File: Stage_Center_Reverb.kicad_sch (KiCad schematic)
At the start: 43 parts, among them J1 Input, J2 Output, J3 ToTank, J4 FromTank, J5 DC9V, Q1 2N3906, SW1 SW_SPDT, SW2 SW_SPDT, SW3 SW_SPDT, SW4 kill, U1 TL072, U2 TL072, U3 MAX1044

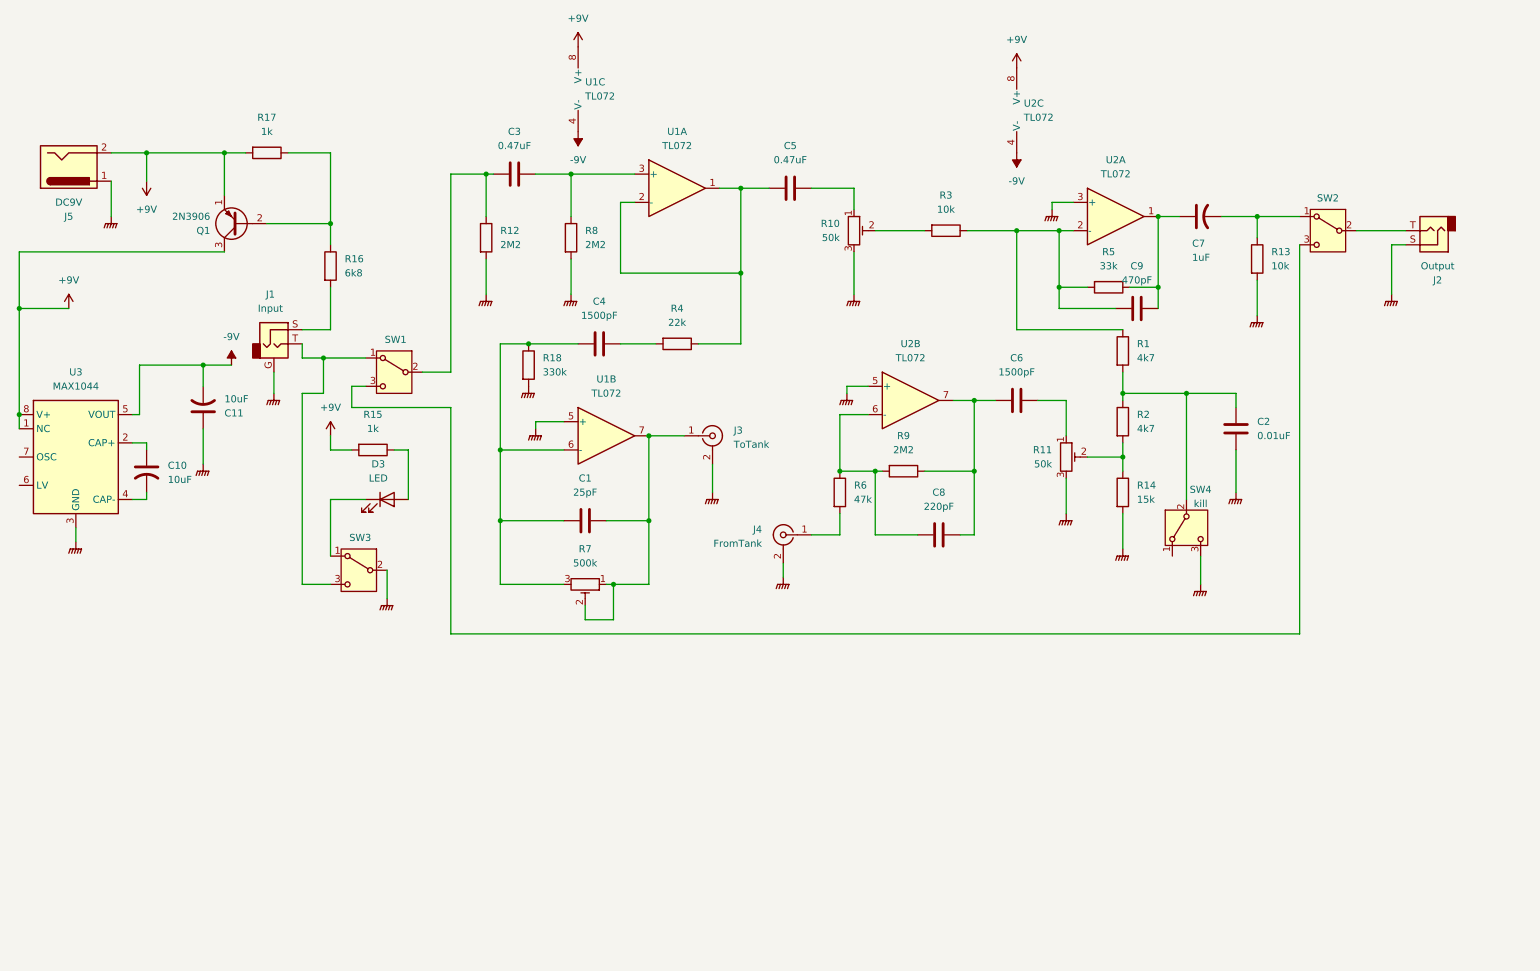
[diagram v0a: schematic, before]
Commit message: 電源部分を変更
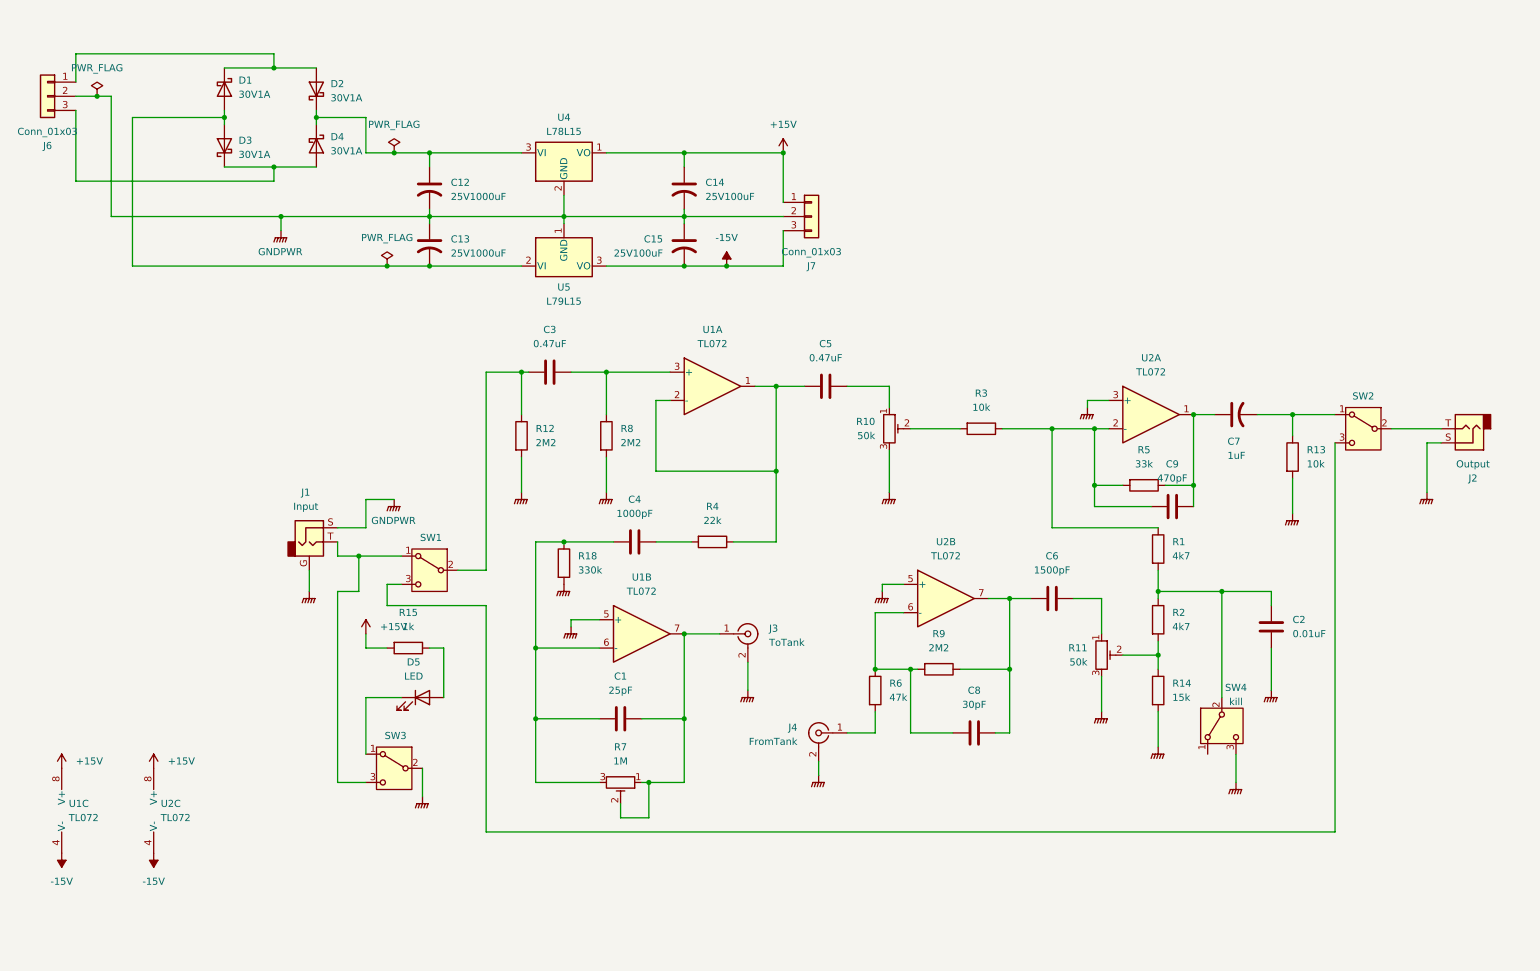
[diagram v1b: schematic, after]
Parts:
- removed C10, C11: 10uF, Capacitor_THT:CP_Radial_D6.3mm_P2.50mm, symbol Device:C_US
- removed J5: DC9V, symbol Connector:Jack-DC
- removed Q1: 2N3906, Package_TO_SOT_THT:TO-92_Inline, symbol Transistor_BJT:2N3906
- removed R16: 6k8, Resistor_THT:R_Axial_DIN0207_L6.3mm_D2.5mm_P7.62mm_Horizontal, symbol Device:R
- removed R17: 1k, Resistor_THT:R_Axial_DIN0207_L6.3mm_D2.5mm_P7.62mm_Horizontal, symbol Device:R
- removed U3: MAX1044, Package_DIP:DIP-8_W7.62mm_Socket, symbol Regulator_SwitchedCapacitor:MAX1044
- added C12, C13: 25V1000uF, Capacitor_THT:CP_Radial_D10.0mm_P5.00mm, symbol Device:C_US
- added C14, C15: 25V100uF, Capacitor_THT:CP_Radial_D7.5mm_P2.50mm, symbol Device:C_US
- added D1, D2, D3, D4: 30V1A, Diode_THT:D_DO-41_SOD81_P10.16mm_Horizontal, symbol Diode:1N5817
- added J6, J7: Conn_01x03, Connector_JST:JST_XH_B3B-XH-A_1x03_P2.50mm_Vertical, symbol Connector_Generic:Conn_01x03
- added U4: L78L15, Package_TO_SOT_THT:TO-92_Inline_Wide, symbol Regulator_Linear:L78L12_TO92
- added U5: L79L15, Package_TO_SOT_THT:TO-92_Inline_Wide, symbol Regulator_Linear:L79L12_TO92
- C4: value 1500pF -> 1000pF
- C8: value 220pF -> 30pF
- R7: value 500k -> 1M
- renumbered D3 to D5
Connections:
- net GNDPWR: now also J1.S, C12.2, C13.1, C14.2, C15.1, J6.2 (Pin_2), J7.2 (Pin_2), U4.2 (GND), U5.1 (GND)
- net +9V renamed +15V
- net +15V: now also C14.1, J7.1 (Pin_1), U4.1 (VO)
- net -9V renamed -15V
- net -15V: now also C15.2, J7.3 (Pin_3), U5.3 (VO)
- new net: C12.1, D2.1 (K), D4.1 (K), U4.3 (VI)
- new net: D1.1 (K), D2.2 (A), J6.1 (Pin_1)
- new net: C13.2, D1.2 (A), D3.2 (A), U5.2 (VI)
- new net: D3.1 (K), D4.2 (A), J6.3 (Pin_3)
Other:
- moved on the sheet: C1, C2, C3, C4, C5, C6, C7, C8, C9, D5, J1, J2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

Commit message: パーツを小型化したフットプリント
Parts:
- C2: footprint @MyLibrary:7.5_3.5_p5.0 -> Capacitor_THT:C_Rect_L7.2mm_W2.5mm_P5.00mm_FKS2_FKP2_MKS2_MKP2
- C3, C5, C6: footprint @MyLibrary:7.5_3.5_p5.0 -> Capacitor_THT:C_Rect_L7.2mm_W3.5mm_P5.00mm_FKS2_FKP2_MKS2_MKP2
- C4: footprint @MyLibrary:7.5_3.5_p5.0 -> Capacitor_THT:C_Disc_D6.0mm_W2.5mm_P5.00mm
- C7: footprint @MyLibrary:10.5_5.0_p7.5 -> Capacitor_THT:C_Rect_L10.3mm_W5.0mm_P7.50mm_MKS4
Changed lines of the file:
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@@
 			)
 		)
-		(property "Footprint" "@MyLibrary:7.5_3.5_p5.0"
+		(property "Footprint" "Capacitor_THT:C_Rect_L7.2mm_W3.5mm_P5.00mm_FKS2_FKP2_MKS2_MKP2"
 			(at 167.64 80.3148 0)
 			(effects
@@
 			)
 		)
-		(property "Footprint" "@MyLibrary:10.5_5.0_p7.5"
+		(property "Footprint" "Capacitor_THT:C_Rect_L10.3mm_W5.0mm_P7.50mm_MKS4"
 			(at 237.49 86.36 0)
 			(effects
@@
 			)
 		)
-		(property "Footprint" "@MyLibrary:7.5_3.5_p5.0"
+		(property "Footprint" "Capacitor_THT:C_Rect_L7.2mm_W3.5mm_P5.00mm_FKS2_FKP2_MKS2_MKP2"
 			(at 208.28 118.4148 0)
 			(effects
@@
 			)
 		)
-		(property "Footprint" "@MyLibrary:7.5_3.5_p5.0"
+		(property "Footprint" "Capacitor_THT:C_Rect_L7.2mm_W2.5mm_P5.00mm_FKS2_FKP2_MKS2_MKP2"
 			(at 244.8052 128.27 0)
 			(effects
@@
 			)
 		)
-		(property "Footprint" "@MyLibrary:7.5_3.5_p5.0"
+		(property "Footprint" "Capacitor_THT:C_Disc_D6.0mm_W2.5mm_P5.00mm"
 			(at 133.35 108.2548 0)
 			(effects
@@
 			)
 		)
-		(property "Footprint" "@MyLibrary:7.5_3.5_p5.0"
+		(property "Footprint" "Capacitor_THT:C_Rect_L7.2mm_W3.5mm_P5.00mm_FKS2_FKP2_MKS2_MKP2"
 			(at 118.11 77.7748 0)
 			(effects

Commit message: フットプリント修正、LEDの抵抗を可変に変更
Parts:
- removed R15: 1k, Resistor_THT:R_Axial_DIN0207_L6.3mm_D2.5mm_P7.62mm_Horizontal, symbol Device:R
- added RV1: 1k, Potentiometer_THT:Potentiometer_Vishay_T73YP_Vertical, symbol Device:R_Potentiometer_Trim
- renumbered R7 to RV2, R10 to RV3, R11 to RV4
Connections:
- net +15V: now also RV1.2
- net GNDPWR: now also RV1.1
- net at D5.2 (A): now also RV1.3
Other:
- moved on the sheet: D5, SW3
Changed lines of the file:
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@@
 	(wire
 		(pts
-			(xy 81.28 137.16) (xy 81.28 147.32)
+			(xy 81.28 144.78) (xy 81.28 154.94)
 		)
 		(stroke
@@
 	(wire
 		(pts
-			(xy 91.44 149.86) (xy 91.44 154.94)
+			(xy 91.44 157.48) (xy 91.44 162.56)
 		)
 		(stroke
@@
 	(wire
 		(pts
-			(xy 76.2 118.11) (xy 76.2 152.4)
-		)
-		(stroke
-			(width 0)
-			(type default)
-		)
-	)
-	(wire
-		(pts
-			(xy 87.63 137.16) (xy 81.28 137.16)
+			(xy 87.63 144.78) (xy 81.28 144.78)
 		)
 		(stroke
@@
 	(wire
 		(pts
+			(xy 88.9 124.46) (xy 95.25 124.46)
+		)
+		(stroke
+			(width 0)
+			(type default)
+		)
+	)
+	(wire
+		(pts
 			(xy 86.36 39.37) (xy 92.71 39.37)
 		)
@@
 	(wire
 		(pts
-			(xy 92.71 128.27) (xy 95.25 128.27)
+			(xy 187.96 132.08) (xy 196.85 132.08)
 		)
 		(stroke
@@
 	(wire
 		(pts
-			(xy 187.96 132.08) (xy 196.85 132.08)
+			(xy 76.2 118.11) (xy 76.2 160.02)
 		)
 		(stroke
@@
 	(wire
 		(pts
-			(xy 95.25 128.27) (xy 95.25 137.16)
+			(xy 95.25 124.46) (xy 95.25 144.78)
 		)
 		(stroke
@@
 	(wire
 		(pts
-			(xy 76.2 152.4) (xy 81.28 152.4)
+			(xy 76.2 160.02) (xy 81.28 160.02)
 		)
 		(stroke
@@
 		(dnp no)
 		(fields_autoplaced yes)
-		(property "Reference" "R11"
+		(property "Reference" "RV4"
 			(at 210.82 128.2699 0)
 			(effects
@@
 			(project "Stage_Center_Reverb"
 				(path "/bb175fc0-f13d-4415-8630-2bbdc9c8566e"
-					(reference "R11")
+					(reference "RV4")
 					(unit 1)
 				)
@@
 	(symbol
 		(lib_id "power:GNDPWR")
+		(at 88.9 132.08 0)
+		(unit 1)
+		(exclude_from_sim no)
+		(in_bom yes)
+		(on_board yes)
+		(dnp no)
+		(fields_autoplaced yes)
+		(property "Reference" "#PWR02"
+			(at 88.9 137.16 0)
+			(effects
+				(font
+					(size 1.27 1.27)
+				)
+				(hide yes)
+			)
+		)
+		(property "Value" "GNDPWR"
+			(at 88.773 135.89 0)
+			(effects
+				(font
+					(size 1.27 1.27)
+				)
+				(hide yes)
+			)
+		)
+		(property "Footprint" ""
+			(at 88.9 133.35 0)
+			(effects
+				(font
+					(size 1.27 1.27)
+				)
+				(hide yes)
+			)
+		)
+		(property "Datasheet" ""
+			(at 88.9 133.35 0)
+			(effects
+				(font
+					(size 1.27 1.27)
+				)
+				(hide yes)
+			)
+		)
+		(property "Description" "Power symbol creates a global label with name \"GNDPWR\" , global ground"
+			(at 88.9 132.08 0)
+			(effects
+				(font
+					(size 1.27 1.27)
+				)
+				(hide yes)
+			)
+		)
+		(pin "1"
+		)
+		(instances
+			(project "Stage_Center_Reverb"
+				(path "/bb175fc0-f13d-4415-8630-2bbdc9c8566e"
+					(reference "#PWR02")
+					(unit 1)
+				)
+			)
+		)
+	)
+	(symbol
+		(lib_id "power:GNDPWR")
 		(at 116.84 116.84 0)
 		(unit 1)
@@
 	(symbol
 		(lib_id "Device:R")
-		(at 88.9 128.27 270)
-		(unit 1)
-		(exclude_from_sim no)
-		(in_bom yes)
-		(on_board yes)
-		(dnp no)
-		(fields_autoplaced yes)
-		(property "Reference" "R15"
-			(at 88.9 121.92 90)
-			(effects
-				(font
-					(size 1.27 1.27)
-				)
-			)
-		)
-		(property "Value" "1k"
-			(at 88.9 124.46 90)
-			(effects
-				(font
-					(size 1.27 1.27)
-				)
-			)
-		)
-		(property "Footprint" "Resistor_THT:R_Axial_DIN0207_L6.3mm_D2.5mm_P7.62mm_Horizontal"
-			(at 88.9 126.492 90)
-			(effects
-				(font
-					(size 1.27 1.27)
-				)
-				(hide yes)
-			)
-		)
-		(property "Datasheet" "~"
-			(at 88.9 128.27 0)
-			(effects
-				(font
-					(size 1.27 1.27)
-				)
-				(hide yes)
-			)
-		)
-		(property "Description" "Resistor"
-			(at 88.9 128.27 0)
-			(effects
-				(font
-					(size 1.27 1.27)
-				)
-				(hide yes)
-			)
-		)
-		(pin "2"
-		)
-		(pin "1"
-		)
-		(instances
-			(project "Stage_Center_Reverb"
-				(path "/bb175fc0-f13d-4415-8630-2bbdc9c8566e"
-					(reference "R15")
-					(unit 1)
-				)
-			)
-		)
-	)
-	(symbol
-		(lib_id "Device:R")
 		(at 191.77 88.9 270)
 		(unit 1)
@@
 		(dnp no)
 		(fields_autoplaced yes)
-		(property "Reference" "R10"
+		(property "Reference" "RV3"
 			(at 172.72 87.6299 0)
 			(effects
@@
 			(project "Stage_Center_Reverb"
 				(path "/bb175fc0-f13d-4415-8630-2bbdc9c8566e"
-					(reference "R10")
+					(reference "RV3")
 					(unit 1)
 				)
@@
 		(on_board yes)
 		(dnp no)
-		(fields_autoplaced yes)
 		(property "Reference" "#PWR08"
 			(at 81.28 129.54 0)
@@
 		)
 		(property "Value" "+15V"
-			(at 83.82 124.4599 0)
+			(at 77.216 122.174 0)
 			(effects
 				(font
@@
 	(symbol
 		(lib_id "Switch:SW_SPDT")
-		(at 86.36 149.86 0)
+		(at 86.36 157.48 0)
 		(mirror y)
 		(unit 1)
@@
 		(dnp no)
 		(property "Reference" "SW3"
-			(at 86.614 144.018 0)
+			(at 86.614 151.638 0)
 			(effects
 				(font
@@
 		)
 		(property "Value" "SW_SPDT"
-			(at 86.36 143.51 0)
+			(at 86.36 151.13 0)
 			(effects
 				(font
@@
 		)
 		(property "Footprint" ""
-			(at 86.36 149.86 0)
+			(at 86.36 157.48 0)
 			(effects
 				(font
@@
 		)
 		(property "Datasheet" "~"
-			(at 86.36 157.48 0)
+			(at 86.36 165.1 0)
 			(effects
 				(font
@@
 		)
 		(property "Description" "Switch, single pole double throw"
-			(at 86.36 149.86 0)
+			(at 86.36 157.48 0)
 			(effects
 				(font
@@
 	(symbol
 		(lib_id "Device:LED")
-		(at 91.44 137.16 0)
+		(at 91.44 144.78 0)
 		(unit 1)
 		(exclude_from_sim no)
@@
 		(fields_autoplaced yes)
 		(property "Reference" "D5"
-			(at 89.8525 130.81 0)
+			(at 89.8525 138.43 0)
 			(effects
 				(font
@@
 		)
 		(property "Value" "LED"
-			(at 89.8525 133.35 0)
+			(at 89.8525 140.97 0)
 			(effects
 				(font
@@
 		)
 		(property "Footprint" ""
-			(at 91.44 137.16 0)
+			(at 91.44 144.78 0)
 			(effects
 				(font
@@
 		)
 		(property "Datasheet" "~"
-			(at 91.44 137.16 0)
+			(at 91.44 144.78 0)
 			(effects
 				(font
@@
 		)
 		(property "Description" "Light emitting diode"
-			(at 91.44 137.16 0)
+			(at 91.44 144.78 0)
 			(effects
 				(font
@@
 		)
 		(property "Sim.Pins" "1=K 2=A"
-			(at 91.44 137.16 0)
+			(at 91.44 144.78 0)
 			(effects
 				(font
@@
 	(symbol
 		(lib_id "power:GNDPWR")
-		(at 91.44 154.94 0)
+		(at 91.44 162.56 0)
 		(unit 1)
 		(exclude_from_sim no)
@@
 		(fields_autoplaced yes)
 		(property "Reference" "#PWR09"
-			(at 91.44 160.02 0)
+			(at 91.44 167.64 0)
 			(effects
 				(font
@@
 		)
 		(property "Value" "GNDPWR"
-			(at 91.313 158.75 0)
+			(at 91.313 166.37 0)
 			(effects
 				(font
@@
 		)
 		(property "Footprint" ""
-			(at 91.44 156.21 0)
+			(at 91.44 163.83 0)
 			(effects
 				(font
@@
 		)
 		(property "Datasheet" ""
-			(at 91.44 156.21 0)
+			(at 91.44 163.83 0)
 			(effects
 				(font
@@
 		)
 		(property "Description" "Power symbol creates a global label with name \"GNDPWR\" , global ground"
-			(at 91.44 154.94 0)
+			(at 91.44 162.56 0)
 			(effects
 				(font
@@
 		(dnp no)
 		(fields_autoplaced yes)
-		(property "Reference" "R7"
+		(property "Reference" "RV2"
 			(at 127 146.05 90)
 			(effects
@@
 			(project ""
 				(path "/bb175fc0-f13d-4415-8630-2bbdc9c8566e"
-					(reference "R7")
+					(reference "RV2")
 					(unit 1)
 				)
@@
 					(unit 1)
 				)
+			)
+		)
+	)
+	(symbol
+		(lib_id "Device:R_Potentiometer_Trim")
+		(at 88.9 128.27 180)
+		(unit 1)
+		(exclude_from_sim no)
+		(in_bom yes)
+		(on_board yes)
+		(dnp no)
+		(property "Reference" "RV1"
+			(at 91.44 126.9999 0)
+			(effects
+				(font
+					(size 1.27 1.27)
+				)
+				(justify right)
+			)
+		)
+		(property "Value" "1k"
+			(at 91.44 129.5399 0)
+			(effects
+				(font
+					(size 1.27 1.27)
+				)
+				(justify right)
+			)
+		)
+		(property "Footprint" "Potentiometer_THT:Potentiometer_Vishay_T73YP_Vertical"
+			(at 88.9 128.27 0)
+			(effects
+				(font
+					(size 1.27 1.27)
+				)
+				(hide yes)
+			)
+		)
+		(property "Datasheet" "~"
+			(at 88.9 128.27 0)
+			(effects
+				(font
+					(size 1.27 1.27)
+				)
+				(hide yes)
+			)
+		)
+		(property "Description" "Trim-potentiometer"
+			(at 88.9 128.27 0)
+			(effects
+				(font
+					(size 1.27 1.27)
+				)
+				(hide yes)
+			)
+		)
+		(pin "1"
+		)
+		(pin "2"
+		)
+		(pin "3"
+		)
+		(instances
+			(project ""
+				(path "/bb175fc0-f13d-4415-8630-2bbdc9c8566e"
+					(reference "RV1")
+					(unit 1)
+				)
